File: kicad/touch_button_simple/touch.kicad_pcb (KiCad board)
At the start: 2 copper layers, 15 x 15 mm, 2 parts, among them J1 CONN_01X02

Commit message: update
- fix pcb
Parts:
- moved J1 2.79 mm to (157.5, 98.3)
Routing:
- net GND: track 17.0 -> 17.8 mm
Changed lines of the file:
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@@
-(kicad_pcb (version 4) (host pcbnew 4.0.7)
+(kicad_pcb (version 4) (host pcbnew 4.0.6)
   (general
     (links 25)
@@
     (thickness 1.6)
     (drawings 6)
-    (tracks 11)
+    (tracks 13)
     (zones 0)
     (modules 2)
@@
     (fp_line (start -7 -7) (end 7 -7) (layer F.SilkS) (width 0.15))
     (fp_line (start -7 7) (end -7 -7) (layer F.SilkS) (width 0.15))
+    (pad 2 smd oval (at 5.334 2.032) (size 2 4) (layers F.Cu F.Paste F.Mask)
+      (net 1 "Net-(J1-Pad1)"))
+    (pad 1 smd oval (at -5.334 -0.508) (size 2 4) (layers F.Cu F.Paste F.Mask)
+      (net 2 GND))
     (pad 1 smd oval (at 1.524 1.778) (size 4 2) (layers F.Cu F.Paste F.Mask)
       (net 2 GND))
@@
     (pad 2 smd oval (at 5.334 0) (size 2 4) (layers F.Cu F.Paste F.Mask)
       (net 1 "Net-(J1-Pad1)"))
-    (pad 2 smd oval (at 5.334 2.032) (size 2 4) (layers F.Cu F.Paste F.Mask)
+    (pad 2 smd oval (at 5.334 2.286) (size 2 4) (layers F.Cu F.Paste F.Mask)
       (net 1 "Net-(J1-Pad1)"))
     (pad 2 smd oval (at 5.334 4.318) (size 2 4) (layers F.Cu F.Paste F.Mask)
@@
     (pad 1 smd oval (at -5.334 0.254) (size 2 4) (layers F.Cu F.Paste F.Mask)
       (net 2 GND))
-    (pad 1 smd oval (at -5.334 -2.032) (size 2 4) (layers F.Cu F.Paste F.Mask)
+    (pad 1 smd oval (at -5.334 -2.54) (size 2 4) (layers F.Cu F.Paste F.Mask)
       (net 2 GND))
     (pad 1 smd oval (at 1.778 -5.334) (size 4 2) (layers F.Cu F.Paste F.Mask)
@@
   )
   (module touch_conn (layer B.Cu)
-    (at 157.48 101.092 90)
+    (at 157.5435 98.298 90)
     (fp_text reference J1 (at 0 -7.112 90) (layer B.Fab)
       (effects (font (size 1 1) (thickness 0.15)) (justify mirror))
@@
       (effects (font (size 1 1) (thickness 0.15)) (justify mirror))
     )
-    (pad 2 smd rect (at 0 -4 90) (size 6 4) (layers B.Cu B.Paste B.Mask)
-      (net 2 GND))
-    (pad 1 smd rect (at 0 4 90) (size 6 4) (layers B.Cu B.Paste B.Mask)
+    (pad 2 smd rect (at 0 -4 90) (size 10 4) (layers B.Cu B.Paste B.Mask)
+      (net 2 GND))
+    (pad 1 smd rect (at 0 4 90) (size 10 4) (layers B.Cu B.Paste B.Mask)
       (net 1 "Net-(J1-Pad1)"))
   )
@@
   (gr_line (start 165 90) (end 165 105) (angle 90) (layer Edge.Cuts) (width 0.15))
   (gr_line (start 150 90) (end 150 105) (angle 90) (layer Edge.Cuts) (width 0.15))
-  (segment (start 161.48 101.092) (end 161.48 93.917) (width 0.25) (layer B.Cu) (net 1) (status 400000))
-  (segment (start 162.814 92.583) (end 162.814 95.504) (width 0.25) (layer F.Cu) (net 1) (status 800000))
+  (segment (start 161.48 101.092) (end 161.48 93.917) (width 0.25) (layer B.Cu) (net 1))
+  (segment (start 162.814 92.583) (end 162.814 95.504) (width 0.25) (layer F.Cu) (net 1))
   (segment (start 163.068 92.329) (end 162.814 92.583) (width 0.25) (layer F.Cu) (net 1))
   (via (at 163.068 92.329) (size 0.6) (drill 0.4) (layers F.Cu B.Cu) (net 1))
   (segment (start 161.48 93.917) (end 163.068 92.329) (width 0.25) (layer B.Cu) (net 1))
-  (segment (start 162.814 95.504) (end 161.798 95.758) (width 0.25) (layer F.Cu) (net 1) (status C00000))
-  (segment (start 153.48 101.092) (end 153.48 100.266) (width 0.25) (layer B.Cu) (net 2) (status C00000))
-  (segment (start 153.48 100.266) (end 162.433 91.313) (width 0.25) (layer B.Cu) (net 2) (status 400000))
+  (segment (start 162.814 95.504) (end 161.798 95.758) (width 0.25) (layer F.Cu) (net 1))
+  (segment (start 162.433 91.313) (end 157.6705 91.313) (width 0.25) (layer B.Cu) (net 2))
+  (segment (start 159.258 92.202) (end 161.544 92.202) (width 0.25) (layer F.Cu) (net 2))
+  (segment (start 162.433 91.313) (end 161.544 92.202) (width 0.25) (layer F.Cu) (net 2))
   (via (at 162.433 91.313) (size 0.6) (drill 0.4) (layers F.Cu B.Cu) (net 2))
-  (segment (start 162.433 91.313) (end 161.544 92.202) (width 0.25) (layer F.Cu) (net 2))
-  (segment (start 161.544 92.202) (end 159.258 92.202) (width 0.25) (layer F.Cu) (net 2) (status 800000))
+  (segment (start 157.6705 91.313) (end 153.5435 95.44) (width 0.25) (layer B.Cu) (net 2) (status 800000))
+  (segment (start 153.5435 95.44) (end 153.5435 98.298) (width 0.25) (layer B.Cu) (net 2) (status C00000))
+  (segment (start 153.48 101.092) (end 153.48 100.266) (width 0.25) (layer B.Cu) (net 2))
 )

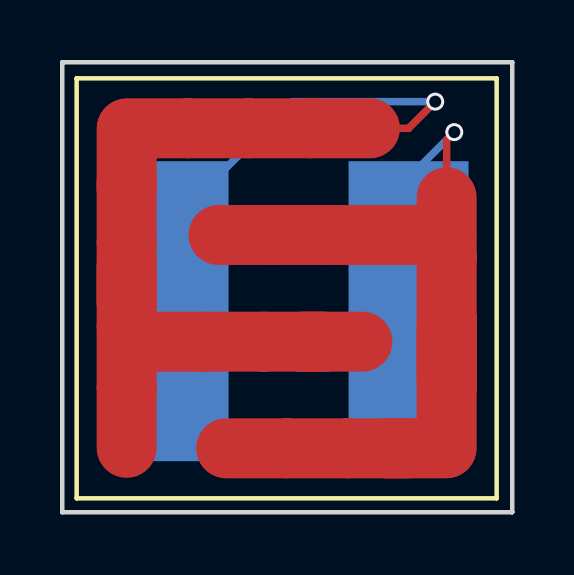
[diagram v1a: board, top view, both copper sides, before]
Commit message: update
better touch button pad
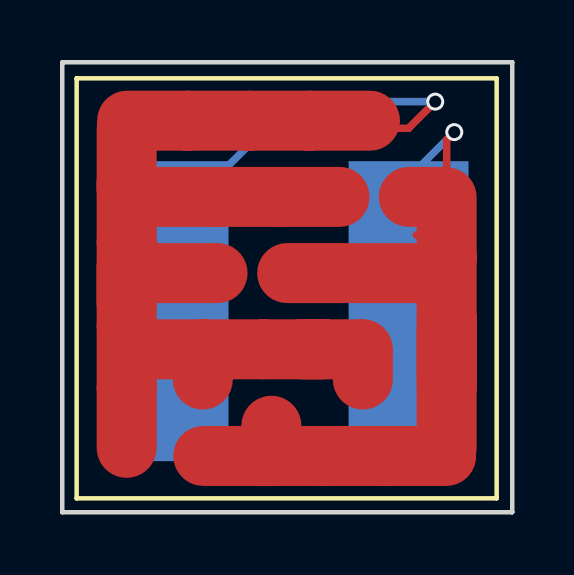
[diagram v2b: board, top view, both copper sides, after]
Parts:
- JP1: footprint touch_zig -> Touch_conn:touch_zig_pro
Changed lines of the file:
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@@
 (kicad_pcb (version 4) (host pcbnew 4.0.6)
   (general
-    (links 25)
-    (no_connects 18)
-    (area 149.924999 89.924999 165.075001 105.075001)
+    (links 33)
+    (no_connects 20)
+    (area 138.033002 82.704659 165.075001 108.263)
     (thickness 1.6)
     (drawings 6)
@@
     (add_net "Net-(J1-Pad1)")
   )
-  (module touch_zig (layer F.Cu)
+  (module touch_conn (layer B.Cu)
+    (at 157.5435 98.298 90)
+    (fp_text reference J1 (at 0 -7.112 90) (layer B.Fab)
+      (effects (font (size 1 1) (thickness 0.15)) (justify mirror))
+    )
+    (fp_text value CONN_01X02 (at 0 -8.89 90) (layer B.Fab)
+      (effects (font (size 1 1) (thickness 0.15)) (justify mirror))
+    )
+    (pad 2 smd rect (at 0 -4 90) (size 10 4) (layers B.Cu B.Paste B.Mask)
+      (net 2 GND))
+    (pad 1 smd rect (at 0 4 90) (size 10 4) (layers B.Cu B.Paste B.Mask)
+      (net 1 "Net-(J1-Pad1)"))
+  )
+  (module Touch_conn:touch_zig_pro (layer F.Cu)
     (at 157.48 97.536)
     (fp_text reference JP1 (at 0 9.652) (layer F.Fab)
@@
     (fp_line (start -7 -7) (end 7 -7) (layer F.SilkS) (width 0.15))
     (fp_line (start -7 7) (end -7 -7) (layer F.SilkS) (width 0.15))
+    (pad 1 smd oval (at 2.54 2.54) (size 2 3) (layers F.Cu F.Paste F.Mask)
+      (net 2 GND))
+    (pad 2 smd oval (at -0.508 5.08) (size 2 3) (layers F.Cu F.Paste F.Mask)
+      (net 1 "Net-(J1-Pad1)"))
+    (pad 1 smd oval (at -2.794 2.54) (size 2 3) (layers F.Cu F.Paste F.Mask)
+      (net 2 GND))
+    (pad 1 smd oval (at 0.762 -3.048) (size 4 2) (layers F.Cu F.Paste F.Mask)
+      (net 2 GND))
+    (pad 1 smd oval (at -1.27 -3.048) (size 4 2) (layers F.Cu F.Paste F.Mask)
+      (net 2 GND))
+    (pad 2 smd oval (at 1.016 -0.508) (size 4 2) (layers F.Cu F.Paste F.Mask)
+      (net 1 "Net-(J1-Pad1)"))
+    (pad 2 smd oval (at -1.778 5.588) (size 4 2) (layers F.Cu F.Paste F.Mask)
+      (net 1 "Net-(J1-Pad1)"))
+    (pad 1 smd oval (at -3.302 -3.048) (size 4 2) (layers F.Cu F.Paste F.Mask)
+      (net 2 GND))
+    (pad 2 smd oval (at 4.572 -3.048) (size 3 2) (layers F.Cu F.Paste F.Mask)
+      (net 1 "Net-(J1-Pad1)"))
     (pad 2 smd oval (at 5.334 2.032) (size 2 4) (layers F.Cu F.Paste F.Mask)
       (net 1 "Net-(J1-Pad1)"))
     (pad 1 smd oval (at -5.334 -0.508) (size 2 4) (layers F.Cu F.Paste F.Mask)
       (net 2 GND))
-    (pad 1 smd oval (at 1.524 1.778) (size 4 2) (layers F.Cu F.Paste F.Mask)
-      (net 2 GND))
-    (pad 1 smd oval (at 0.254 1.778) (size 4 2) (layers F.Cu F.Paste F.Mask)
-      (net 2 GND))
-    (pad 1 smd oval (at -1.778 1.778) (size 4 2) (layers F.Cu F.Paste F.Mask)
-      (net 2 GND))
-    (pad 1 smd oval (at -3.81 1.778) (size 4 2) (layers F.Cu F.Paste F.Mask)
-      (net 2 GND))
-    (pad 2 smd oval (at -1.27 -1.778) (size 4 2) (layers F.Cu F.Paste F.Mask)
-      (net 1 "Net-(J1-Pad1)"))
-    (pad 2 smd oval (at 0.254 -1.778) (size 4 2) (layers F.Cu F.Paste F.Mask)
-      (net 1 "Net-(J1-Pad1)"))
-    (pad 2 smd oval (at 2.286 -1.778) (size 4 2) (layers F.Cu F.Paste F.Mask)
-      (net 1 "Net-(J1-Pad1)"))
-    (pad 2 smd oval (at 4.318 -1.778) (size 4 2) (layers F.Cu F.Paste F.Mask)
+    (pad 1 smd oval (at 1.524 2.032) (size 4 2) (layers F.Cu F.Paste F.Mask)
+      (net 2 GND))
+    (pad 1 smd oval (at 0.254 2.032) (size 4 2) (layers F.Cu F.Paste F.Mask)
+      (net 2 GND))
+    (pad 1 smd oval (at -1.778 2.032) (size 4 2) (layers F.Cu F.Paste F.Mask)
+      (net 2 GND))
+    (pad 1 smd oval (at -3.81 2.032) (size 4 2) (layers F.Cu F.Paste F.Mask)
+      (net 2 GND))
+    (pad 1 smd oval (at -3.302 -0.508) (size 4 2) (layers F.Cu F.Paste F.Mask)
+      (net 2 GND))
+    (pad 2 smd oval (at 3.302 -0.508) (size 4 2) (layers F.Cu F.Paste F.Mask)
       (net 1 "Net-(J1-Pad1)"))
     (pad 2 smd oval (at 5.334 -2.032) (size 2 4) (layers F.Cu F.Paste F.Mask)
@@
     (pad 2 smd oval (at 5.334 4.318) (size 2 4) (layers F.Cu F.Paste F.Mask)
       (net 1 "Net-(J1-Pad1)"))
-    (pad 2 smd oval (at 4.318 5.334) (size 4 2) (layers F.Cu F.Paste F.Mask)
-      (net 1 "Net-(J1-Pad1)"))
-    (pad 2 smd oval (at 3.048 5.334) (size 4 2) (layers F.Cu F.Paste F.Mask)
-      (net 1 "Net-(J1-Pad1)"))
-    (pad 2 smd oval (at 1.016 5.334) (size 4 2) (layers F.Cu F.Paste F.Mask)
-      (net 1 "Net-(J1-Pad1)"))
-    (pad 2 smd oval (at -1.016 5.334) (size 4 2) (layers F.Cu F.Paste F.Mask)
+    (pad 2 smd oval (at 2.286 5.588) (size 4 2) (layers F.Cu F.Paste F.Mask)
+      (net 1 "Net-(J1-Pad1)"))
+    (pad 2 smd oval (at 4.318 5.588) (size 4 2) (layers F.Cu F.Paste F.Mask)
+      (net 1 "Net-(J1-Pad1)"))
+    (pad 2 smd oval (at 0.254 5.588) (size 4 2) (layers F.Cu F.Paste F.Mask)
       (net 1 "Net-(J1-Pad1)"))
     (pad 1 smd oval (at -5.334 4.318) (size 2 4) (layers F.Cu F.Paste F.Mask)
@@
     (pad 1 smd oval (at -5.334 -2.54) (size 2 4) (layers F.Cu F.Paste F.Mask)
       (net 2 GND))
-    (pad 1 smd oval (at 1.778 -5.334) (size 4 2) (layers F.Cu F.Paste F.Mask)
-      (net 2 GND))
-    (pad 1 smd oval (at -0.254 -5.334) (size 4 2) (layers F.Cu F.Paste F.Mask)
-      (net 2 GND))
-    (pad 1 smd oval (at -2.286 -5.334) (size 4 2) (layers F.Cu F.Paste F.Mask)
-      (net 2 GND))
-    (pad 1 smd oval (at -4.318 -5.334) (size 4 2) (layers F.Cu F.Paste F.Mask)
+    (pad 1 smd oval (at 1.778 -5.588) (size 4 2) (layers F.Cu F.Paste F.Mask)
+      (net 2 GND))
+    (pad 1 smd oval (at -0.254 -5.588) (size 4 2) (layers F.Cu F.Paste F.Mask)
+      (net 2 GND))
+    (pad 1 smd oval (at -2.286 -5.588) (size 4 2) (layers F.Cu F.Paste F.Mask)
+      (net 2 GND))
+    (pad 1 smd oval (at -4.318 -5.588) (size 4 2) (layers F.Cu F.Paste F.Mask)
       (net 2 GND))
     (pad 1 smd oval (at -5.334 -4.318) (size 2 4) (layers F.Cu F.Paste F.Mask)
       (net 2 GND))
-  )
-  (module touch_conn (layer B.Cu)
-    (at 157.5435 98.298 90)
-    (fp_text reference J1 (at 0 -7.112 90) (layer B.Fab)
-      (effects (font (size 1 1) (thickness 0.15)) (justify mirror))
-    )
-    (fp_text value CONN_01X02 (at 0 -8.89 90) (layer B.Fab)
-      (effects (font (size 1 1) (thickness 0.15)) (justify mirror))
-    )
-    (pad 2 smd rect (at 0 -4 90) (size 10 4) (layers B.Cu B.Paste B.Mask)
-      (net 2 GND))
-    (pad 1 smd rect (at 0 4 90) (size 10 4) (layers B.Cu B.Paste B.Mask)
-      (net 1 "Net-(J1-Pad1)"))
   )
   (gr_line (start 150 90) (end 165 90) (angle 90) (layer Edge.Cuts) (width 0.15))
@@
   (segment (start 162.433 91.313) (end 161.544 92.202) (width 0.25) (layer F.Cu) (net 2))
   (via (at 162.433 91.313) (size 0.6) (drill 0.4) (layers F.Cu B.Cu) (net 2))
-  (segment (start 157.6705 91.313) (end 153.5435 95.44) (width 0.25) (layer B.Cu) (net 2) (status 800000))
-  (segment (start 153.5435 95.44) (end 153.5435 98.298) (width 0.25) (layer B.Cu) (net 2) (status C00000))
+  (segment (start 157.6705 91.313) (end 153.5435 95.44) (width 0.25) (layer B.Cu) (net 2))
+  (segment (start 153.5435 95.44) (end 153.5435 98.298) (width 0.25) (layer B.Cu) (net 2))
   (segment (start 153.48 101.092) (end 153.48 100.266) (width 0.25) (layer B.Cu) (net 2))
 )

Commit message: update
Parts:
- J1: footprint touch_conn -> Touch_conn:touch_conn_cap
- moved J1 0.51 mm to (157.5, 97.8)
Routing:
- net GND: track 17.8 -> 21.9 mm
- net Net-(J1-Pad1): track 13.7 -> 14.4 mm
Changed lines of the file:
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@@
 (kicad_pcb (version 4) (host pcbnew 4.0.6)
   (general
-    (links 33)
-    (no_connects 20)
-    (area 138.033002 82.704659 165.075001 108.263)
+    (links 35)
+    (no_connects 18)
+    (area 149.924999 89.924999 165.075001 105.075001)
     (thickness 1.6)
     (drawings 6)
@@
   )
   (net 0 "")
-  (net 1 "Net-(J1-Pad1)")
-  (net 2 GND)
+  (net 1 GND)
+  (net 2 "Net-(J1-Pad1)")
   (net_class Default "This is the default net class."
     (clearance 0.2)
@@
     (add_net "Net-(J1-Pad1)")
   )
-  (module touch_conn (layer B.Cu)
-    (at 157.5435 98.298 90)
+  (module Touch_conn:touch_conn_cap (layer B.Cu)
+    (at 157.48 97.79 90)
     (fp_text reference J1 (at 0 -7.112 90) (layer B.Fab)
       (effects (font (size 1 1) (thickness 0.15)) (justify mirror))
@@
       (effects (font (size 1 1) (thickness 0.15)) (justify mirror))
     )
-    (pad 2 smd rect (at 0 -4 90) (size 10 4) (layers B.Cu B.Paste B.Mask)
-      (net 2 GND))
-    (pad 1 smd rect (at 0 4 90) (size 10 4) (layers B.Cu B.Paste B.Mask)
-      (net 1 "Net-(J1-Pad1)"))
+    (fp_line (start -4.064 -0.762) (end -4.064 -1.524) (layer B.SilkS) (width 0.4))
+    (fp_line (start -4.064 0.762) (end -4.064 1.524) (layer B.SilkS) (width 0.4))
+    (fp_line (start -4.826 -0.508) (end -3.302 -0.508) (layer B.SilkS) (width 0.4))
+    (fp_line (start -4.826 0.508) (end -3.302 0.508) (layer B.SilkS) (width 0.4))
+    (pad 2 smd rect (at -4.064 -4.064 90) (size 2 4) (layers B.Cu B.Paste B.Mask)
+      (net 1 GND))
+    (pad 1 smd rect (at -4.064 4.064 90) (size 2 4) (layers B.Cu B.Paste B.Mask)
+      (net 2 "Net-(J1-Pad1)"))
+    (pad 2 smd rect (at 2.032 -4.064 90) (size 6 4) (layers B.Cu B.Paste B.Mask)
+      (net 1 GND))
+    (pad 1 smd rect (at 2.032 4.064 90) (size 6 4) (layers B.Cu B.Paste B.Mask)
+      (net 2 "Net-(J1-Pad1)"))
   )
   (module Touch_conn:touch_zig_pro (layer F.Cu)
@@
     (fp_line (start -7 7) (end -7 -7) (layer F.SilkS) (width 0.15))
     (pad 1 smd oval (at 2.54 2.54) (size 2 3) (layers F.Cu F.Paste F.Mask)
-      (net 2 GND))
+      (net 1 GND))
     (pad 2 smd oval (at -0.508 5.08) (size 2 3) (layers F.Cu F.Paste F.Mask)
-      (net 1 "Net-(J1-Pad1)"))
+      (net 2 "Net-(J1-Pad1)"))
     (pad 1 smd oval (at -2.794 2.54) (size 2 3) (layers F.Cu F.Paste F.Mask)
-      (net 2 GND))
-    (pad 1 smd oval (at 0.762 -3.048) (size 4 2) (layers F.Cu F.Paste F.Mask)
-      (net 2 GND))
-    (pad 1 smd oval (at -1.27 -3.048) (size 4 2) (layers F.Cu F.Paste F.Mask)
-      (net 2 GND))
-    (pad 2 smd oval (at 1.016 -0.508) (size 4 2) (layers F.Cu F.Paste F.Mask)
-      (net 1 "Net-(J1-Pad1)"))
+      (net 1 GND))
+    (pad 2 smd oval (at 3.048 -3.048) (size 4 2) (layers F.Cu F.Paste F.Mask)
+      (net 2 "Net-(J1-Pad1)"))
+    (pad 1 smd oval (at -1.524 -3.048) (size 4 2) (layers F.Cu F.Paste F.Mask)
+      (net 1 GND))
+    (pad 2 smd oval (at 1.27 -0.508) (size 4 2) (layers F.Cu F.Paste F.Mask)
+      (net 2 "Net-(J1-Pad1)"))
     (pad 2 smd oval (at -1.778 5.588) (size 4 2) (layers F.Cu F.Paste F.Mask)
-      (net 1 "Net-(J1-Pad1)"))
+      (net 2 "Net-(J1-Pad1)"))
     (pad 1 smd oval (at -3.302 -3.048) (size 4 2) (layers F.Cu F.Paste F.Mask)
-      (net 2 GND))
+      (net 1 GND))
     (pad 2 smd oval (at 4.572 -3.048) (size 3 2) (layers F.Cu F.Paste F.Mask)
-      (net 1 "Net-(J1-Pad1)"))
+      (net 2 "Net-(J1-Pad1)"))
     (pad 2 smd oval (at 5.334 2.032) (size 2 4) (layers F.Cu F.Paste F.Mask)
-      (net 1 "Net-(J1-Pad1)"))
+      (net 2 "Net-(J1-Pad1)"))
     (pad 1 smd oval (at -5.334 -0.508) (size 2 4) (layers F.Cu F.Paste F.Mask)
-      (net 2 GND))
+      (net 1 GND))
     (pad 1 smd oval (at 1.524 2.032) (size 4 2) (layers F.Cu F.Paste F.Mask)
-      (net 2 GND))
+      (net 1 GND))
     (pad 1 smd oval (at 0.254 2.032) (size 4 2) (layers F.Cu F.Paste F.Mask)
-      (net 2 GND))
+      (net 1 GND))
     (pad 1 smd oval (at -1.778 2.032) (size 4 2) (layers F.Cu F.Paste F.Mask)
-      (net 2 GND))
+      (net 1 GND))
     (pad 1 smd oval (at -3.81 2.032) (size 4 2) (layers F.Cu F.Paste F.Mask)
-      (net 2 GND))
+      (net 1 GND))
     (pad 1 smd oval (at -3.302 -0.508) (size 4 2) (layers F.Cu F.Paste F.Mask)
-      (net 2 GND))
+      (net 1 GND))
     (pad 2 smd oval (at 3.302 -0.508) (size 4 2) (layers F.Cu F.Paste F.Mask)
-      (net 1 "Net-(J1-Pad1)"))
+      (net 2 "Net-(J1-Pad1)"))
     (pad 2 smd oval (at 5.334 -2.032) (size 2 4) (layers F.Cu F.Paste F.Mask)
-      (net 1 "Net-(J1-Pad1)"))
+      (net 2 "Net-(J1-Pad1)"))
     (pad 2 smd oval (at 5.334 0) (size 2 4) (layers F.Cu F.Paste F.Mask)
-      (net 1 "Net-(J1-Pad1)"))
+      (net 2 "Net-(J1-Pad1)"))
     (pad 2 smd oval (at 5.334 2.286) (size 2 4) (layers F.Cu F.Paste F.Mask)
-      (net 1 "Net-(J1-Pad1)"))
+      (net 2 "Net-(J1-Pad1)"))
     (pad 2 smd oval (at 5.334 4.318) (size 2 4) (layers F.Cu F.Paste F.Mask)
-      (net 1 "Net-(J1-Pad1)"))
+      (net 2 "Net-(J1-Pad1)"))
     (pad 2 smd oval (at 2.286 5.588) (size 4 2) (layers F.Cu F.Paste F.Mask)
-      (net 1 "Net-(J1-Pad1)"))
+      (net 2 "Net-(J1-Pad1)"))
     (pad 2 smd oval (at 4.318 5.588) (size 4 2) (layers F.Cu F.Paste F.Mask)
-      (net 1 "Net-(J1-Pad1)"))
+      (net 2 "Net-(J1-Pad1)"))
     (pad 2 smd oval (at 0.254 5.588) (size 4 2) (layers F.Cu F.Paste F.Mask)
-      (net 1 "Net-(J1-Pad1)"))
+      (net 2 "Net-(J1-Pad1)"))
     (pad 1 smd oval (at -5.334 4.318) (size 2 4) (layers F.Cu F.Paste F.Mask)
-      (net 2 GND))
+      (net 1 GND))
     (pad 1 smd oval (at -5.334 2.286) (size 2 4) (layers F.Cu F.Paste F.Mask)
-      (net 2 GND))
+      (net 1 GND))
     (pad 1 smd oval (at -5.334 0.254) (size 2 4) (layers F.Cu F.Paste F.Mask)
-      (net 2 GND))
+      (net 1 GND))
     (pad 1 smd oval (at -5.334 -2.54) (size 2 4) (layers F.Cu F.Paste F.Mask)
-      (net 2 GND))
+      (net 1 GND))
     (pad 1 smd oval (at 1.778 -5.588) (size 4 2) (layers F.Cu F.Paste F.Mask)
-      (net 2 GND))
+      (net 1 GND))
     (pad 1 smd oval (at -0.254 -5.588) (size 4 2) (layers F.Cu F.Paste F.Mask)
-      (net 2 GND))
+      (net 1 GND))
     (pad 1 smd oval (at -2.286 -5.588) (size 4 2) (layers F.Cu F.Paste F.Mask)
-      (net 2 GND))
+      (net 1 GND))
     (pad 1 smd oval (at -4.318 -5.588) (size 4 2) (layers F.Cu F.Paste F.Mask)
-      (net 2 GND))
+      (net 1 GND))
     (pad 1 smd oval (at -5.334 -4.318) (size 2 4) (layers F.Cu F.Paste F.Mask)
-      (net 2 GND))
+      (net 1 GND))
   )
   (gr_line (start 150 90) (end 165 90) (angle 90) (layer Edge.Cuts) (width 0.15))
@@
   (gr_line (start 165 90) (end 165 105) (angle 90) (layer Edge.Cuts) (width 0.15))
   (gr_line (start 150 90) (end 150 105) (angle 90) (layer Edge.Cuts) (width 0.15))
-  (segment (start 161.48 101.092) (end 161.48 93.917) (width 0.25) (layer B.Cu) (net 1))
-  (segment (start 162.814 92.583) (end 162.814 95.504) (width 0.25) (layer F.Cu) (net 1))
-  (segment (start 163.068 92.329) (end 162.814 92.583) (width 0.25) (layer F.Cu) (net 1))
-  (via (at 163.068 92.329) (size 0.6) (drill 0.4) (layers F.Cu B.Cu) (net 1))
-  (segment (start 161.48 93.917) (end 163.068 92.329) (width 0.25) (layer B.Cu) (net 1))
-  (segment (start 162.814 95.504) (end 161.798 95.758) (width 0.25) (layer F.Cu) (net 1))
-  (segment (start 162.433 91.313) (end 157.6705 91.313) (width 0.25) (layer B.Cu) (net 2))
-  (segment (start 159.258 92.202) (end 161.544 92.202) (width 0.25) (layer F.Cu) (net 2))
-  (segment (start 162.433 91.313) (end 161.544 92.202) (width 0.25) (layer F.Cu) (net 2))
-  (via (at 162.433 91.313) (size 0.6) (drill 0.4) (layers F.Cu B.Cu) (net 2))
-  (segment (start 157.6705 91.313) (end 153.5435 95.44) (width 0.25) (layer B.Cu) (net 2))
-  (segment (start 153.5435 95.44) (end 153.5435 98.298) (width 0.25) (layer B.Cu) (net 2))
-  (segment (start 153.48 101.092) (end 153.48 100.266) (width 0.25) (layer B.Cu) (net 2))
+  (segment (start 153.416 95.758) (end 153.416 101.854) (width 0.25) (layer B.Cu) (net 1) (status C00000))
+  (segment (start 161.798 91.948) (end 159.258 91.948) (width 0.25) (layer F.Cu) (net 1))
+  (segment (start 162.56 91.186) (end 161.798 91.948) (width 0.25) (layer F.Cu) (net 1))
+  (via (at 162.56 91.186) (size 0.6) (drill 0.4) (layers F.Cu B.Cu) (net 1))
+  (segment (start 155.956 91.186) (end 162.56 91.186) (width 0.25) (layer B.Cu) (net 1))
+  (segment (start 153.416 93.726) (end 155.956 91.186) (width 0.25) (layer B.Cu) (net 1))
+  (segment (start 153.416 95.758) (end 153.416 93.726) (width 0.25) (layer B.Cu) (net 1))
+  (segment (start 161.544 95.758) (end 161.544 101.854) (width 0.25) (layer B.Cu) (net 2) (status C00000))
+  (segment (start 161.544 95.758) (end 161.544 93.726) (width 0.25) (layer B.Cu) (net 2))
+  (segment (start 161.544 93.726) (end 163.322 91.948) (width 0.25) (layer B.Cu) (net 2))
+  (via (at 163.322 91.948) (size 0.6) (drill 0.4) (layers F.Cu B.Cu) (net 2))
+  (segment (start 163.322 91.948) (end 162.814 92.456) (width 0.25) (layer F.Cu) (net 2))
+  (segment (start 162.814 92.456) (end 162.814 95.504) (width 0.25) (layer F.Cu) (net 2))
 )
